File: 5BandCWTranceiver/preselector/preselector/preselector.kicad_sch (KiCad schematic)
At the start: 80 parts, among them J1 Conn_01x06_Male, J2 Conn_01x02_Male, J3 Conn_Coaxial, J4 Conn_Coaxial, J5 Conn_01x02_Male, J6 Conn_01x02_Male, J7 Conn_01x02_Male, J8 Conn_01x02_Male, J9 Conn_Coaxial, K1 G5V-2, K2 G5V-2, K3 G5V-2, K4 G5V-2, K5 G5V-2, Q1 MMBT3904, Q2 MMBT3904, Q3 MMBT3904, Q4 MMBT3904, Q5 MMBT3904

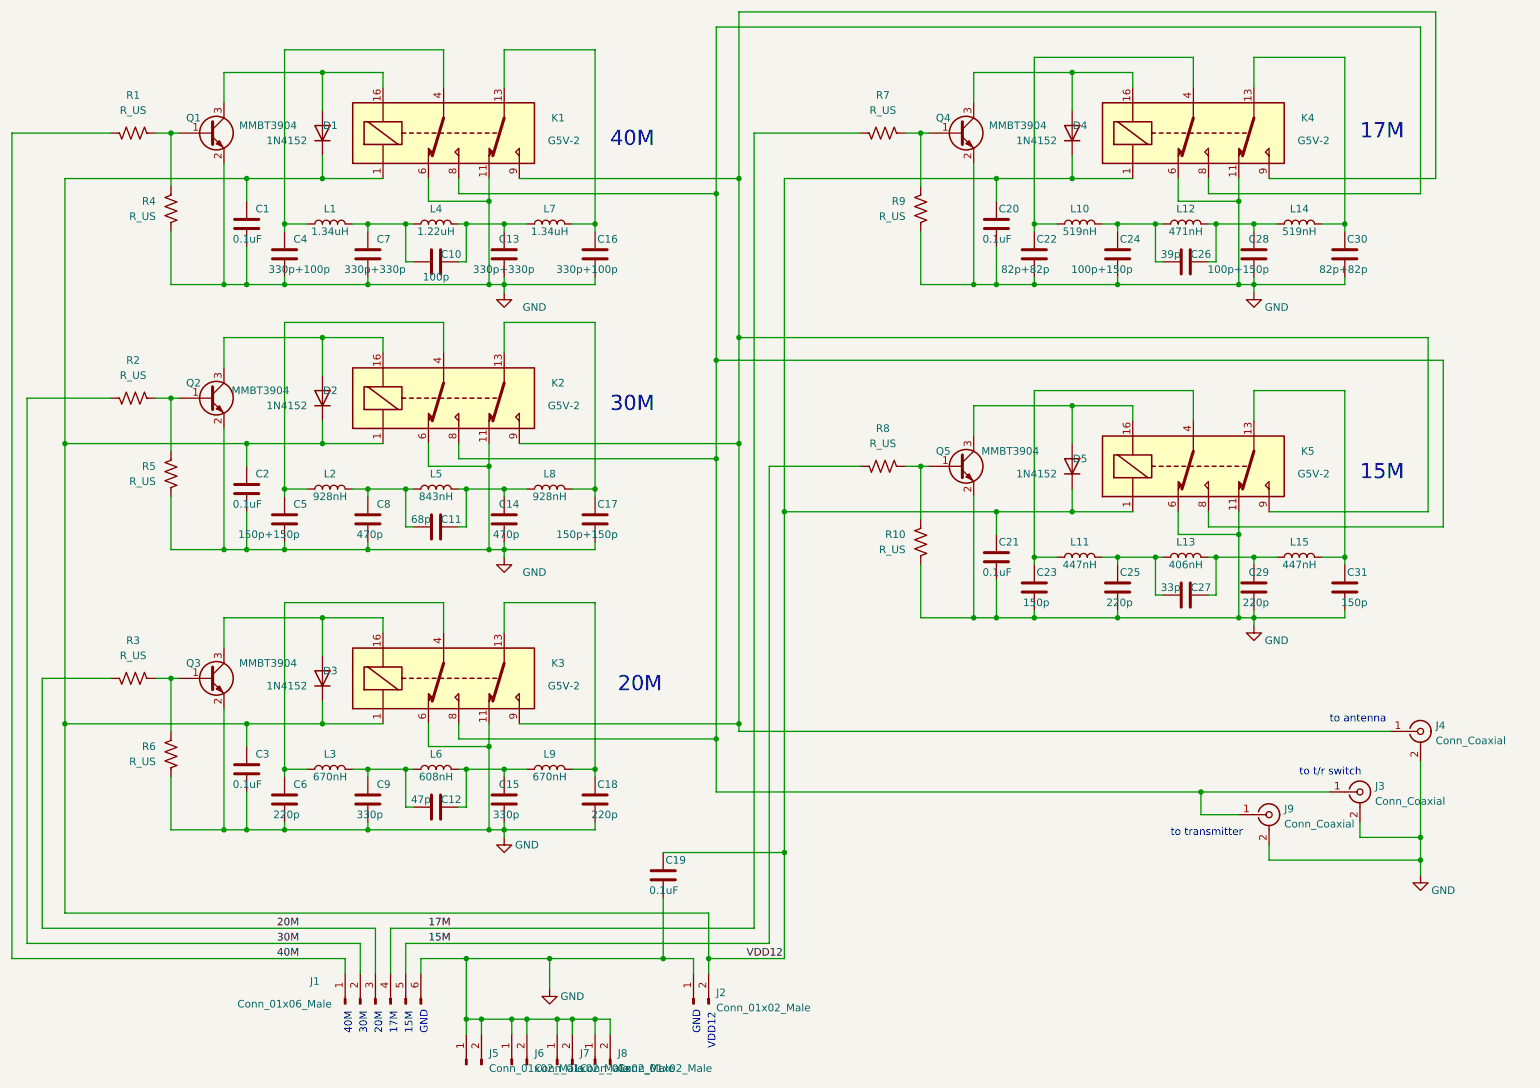
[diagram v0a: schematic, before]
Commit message: Corrected LPF; add Preselector
Fixed circuit design error on LPF regarding relay connections; first pass at adding preselctor schematic
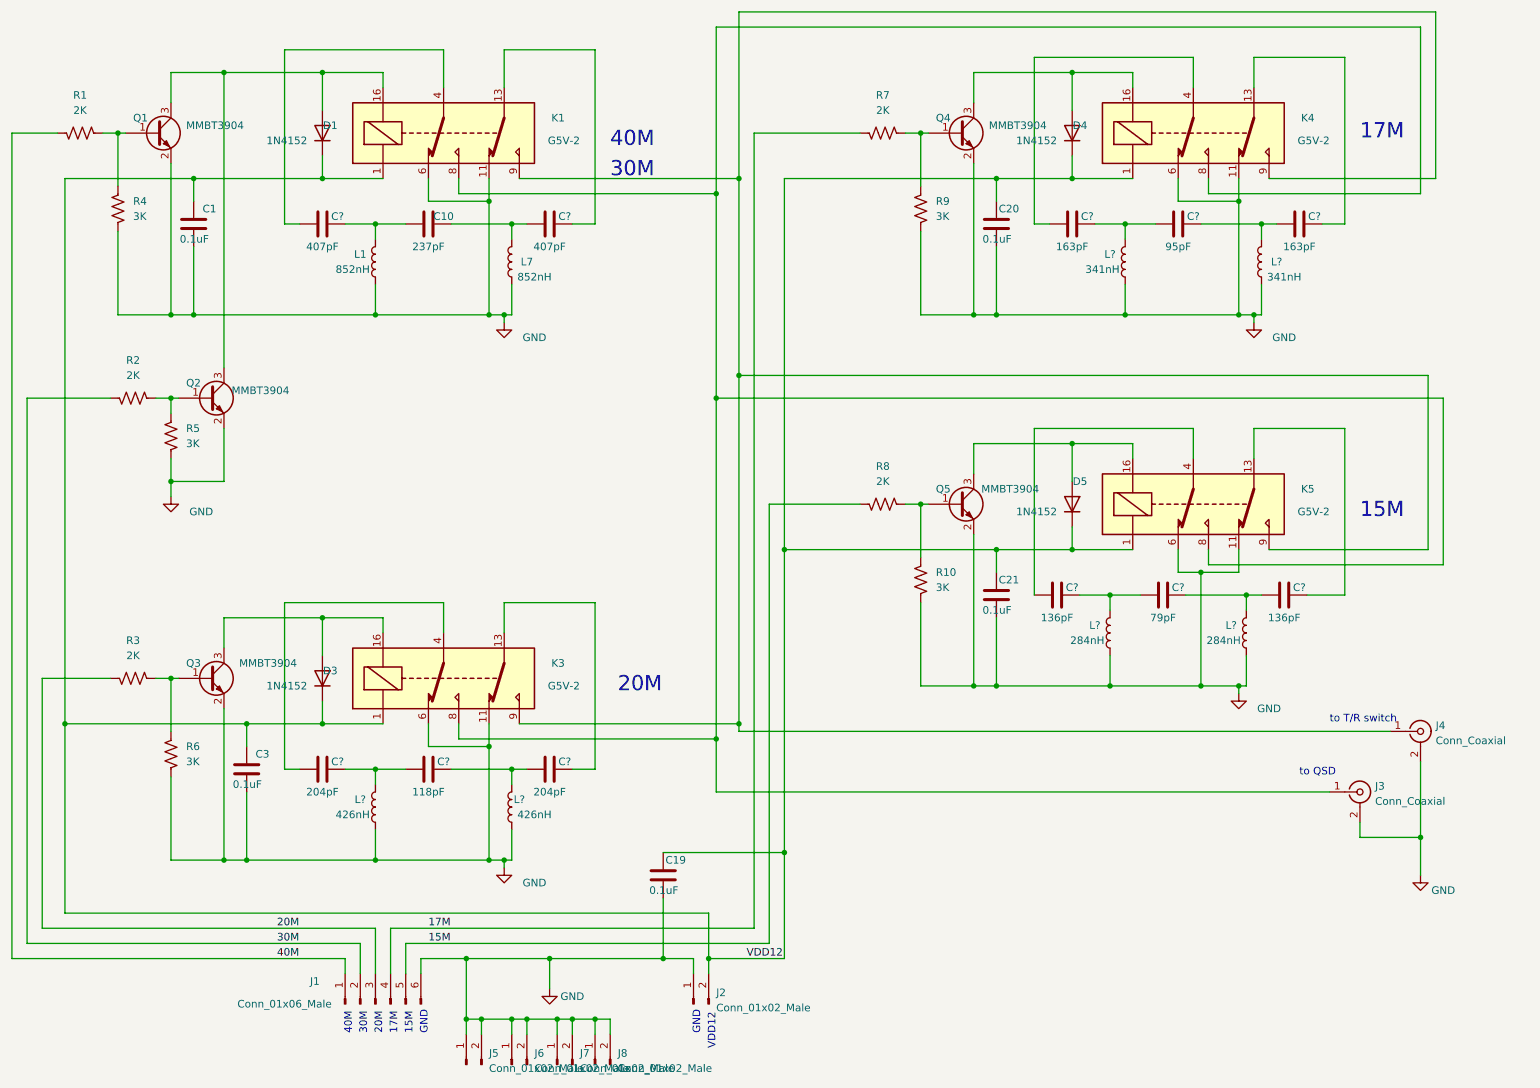
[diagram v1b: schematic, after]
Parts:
- removed C11: 68p, Capacitor_SMD:C_0805_2012Metric_Pad1.18x1.45mm_HandSolder, symbol Device:C
- removed C12: 47p, Capacitor_SMD:C_0805_2012Metric_Pad1.18x1.45mm_HandSolder, symbol Device:C
- removed C13, C7: 330p+330p, Capacitor_SMD:C_0805_2012Metric_Pad1.18x1.45mm_HandSolder, symbol Device:C
- removed C14, C8: 470p, Capacitor_SMD:C_0805_2012Metric_Pad1.18x1.45mm_HandSolder, symbol Device:C
- removed C15, C9: 330p, Capacitor_SMD:C_0805_2012Metric_Pad1.18x1.45mm_HandSolder, symbol Device:C
- removed C16, C4: 330p+100p, Capacitor_SMD:C_0805_2012Metric_Pad1.18x1.45mm_HandSolder, symbol Device:C
- removed C17, C5: 150p+150p, Capacitor_SMD:C_0805_2012Metric_Pad1.18x1.45mm_HandSolder, symbol Device:C
- removed C18, C25, C29, C6: 220p, Capacitor_SMD:C_0805_2012Metric_Pad1.18x1.45mm_HandSolder, symbol Device:C
- removed C2: 0.1uF, Capacitor_SMD:C_0603_1608Metric_Pad1.08x0.95mm_HandSolder, symbol Device:C
- removed C22, C30: 82p+82p, Capacitor_SMD:C_0805_2012Metric_Pad1.18x1.45mm_HandSolder, symbol Device:C
- removed C23, C31: 150p, Capacitor_SMD:C_0805_2012Metric_Pad1.18x1.45mm_HandSolder, symbol Device:C
- removed C24, C28: 100p+150p, Capacitor_SMD:C_0805_2012Metric_Pad1.18x1.45mm_HandSolder, symbol Device:C
- removed C26: 39p, Capacitor_SMD:C_0805_2012Metric_Pad1.18x1.45mm_HandSolder, symbol Device:C
- removed C27: 33p, Capacitor_SMD:C_0805_2012Metric_Pad1.18x1.45mm_HandSolder, symbol Device:C
- removed D2: 1N4152, Diode_THT:D_DO-41_SOD81_P7.62mm_Horizontal, symbol Device:D
- removed J9: Conn_Coaxial, Connector_Coaxial:SMA_Samtec_SMA-J-P-X-ST-EM1_EdgeMount, symbol Connector:Conn_Coaxial
- removed K2: G5V-2, Relay_THT:Relay_DPDT_Omron_G5V-2, symbol Relay:G5V-2
- removed L10, L14: 519nH, Inductor_THT:L_Toroid_Vertical_L13.0mm_W6.5mm_P5.60mm, symbol Device:L
- removed L11, L15: 447nH, Inductor_THT:L_Toroid_Vertical_L13.0mm_W6.5mm_P5.60mm, symbol Device:L
- removed L12: 471nH, Inductor_THT:L_Toroid_Vertical_L13.0mm_W6.5mm_P5.60mm, symbol Device:L
- removed L13: 406nH, Inductor_THT:L_Toroid_Vertical_L13.0mm_W6.5mm_P5.60mm, symbol Device:L
- removed L2, L8: 928nH, Inductor_THT:L_Toroid_Vertical_L13.0mm_W6.5mm_P5.60mm, symbol Device:L
- removed L3, L9: 670nH, Inductor_THT:L_Toroid_Vertical_L13.0mm_W6.5mm_P5.60mm, symbol Device:L
- removed L4: 1.22uH, Inductor_THT:L_Toroid_Vertical_L13.0mm_W6.5mm_P5.60mm, symbol Device:L
- removed L5: 843nH, Inductor_THT:L_Toroid_Vertical_L13.0mm_W6.5mm_P5.60mm, symbol Device:L
- removed L6: 608nH, Inductor_THT:L_Toroid_Vertical_L13.0mm_W6.5mm_P5.60mm, symbol Device:L
- added C? (x2): 204pF, Capacitor_SMD:C_0805_2012Metric_Pad1.18x1.45mm_HandSolder, symbol Device:C
- added C?: 95pF, Capacitor_SMD:C_0805_2012Metric_Pad1.18x1.45mm_HandSolder, symbol Device:C
- added C?: 118pF, Capacitor_SMD:C_0805_2012Metric_Pad1.18x1.45mm_HandSolder, symbol Device:C
- added C? (x2): 136pF, Capacitor_SMD:C_0805_2012Metric_Pad1.18x1.45mm_HandSolder, symbol Device:C
- added C? (x2): 163pF, Capacitor_SMD:C_0805_2012Metric_Pad1.18x1.45mm_HandSolder, symbol Device:C
- added C?: 79pF, Capacitor_SMD:C_0805_2012Metric_Pad1.18x1.45mm_HandSolder, symbol Device:C
- added C? (x2): 407pF, Capacitor_SMD:C_0805_2012Metric_Pad1.18x1.45mm_HandSolder, symbol Device:C
- added L? (x2): 341nH, Inductor_THT:L_Toroid_Vertical_L13.0mm_W6.5mm_P5.60mm, symbol Device:L
- added L? (x2): 426nH, Inductor_THT:L_Toroid_Vertical_L13.0mm_W6.5mm_P5.60mm, symbol Device:L
- added L? (x2): 284nH, Inductor_THT:L_Toroid_Vertical_L13.0mm_W6.5mm_P5.60mm, symbol Device:L
- C10: value 100p -> 237pF
- L1, L7: value 1.34uH -> 852nH
- R1, R2, R3, R7, R8: value R_US -> 2K
- R10, R4, R5, R6, R9: value R_US -> 3K
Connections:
- net GND: now also L1.2, L7.2, L?.2, L?.2, L?.2, L?.2, L?.2, L?.2
- net at K4.13: now also C?.1
- net at K3.13: now also C?.1
- net at K3.4: now also C?.2
- net at C10.1: now also L7.1, C?.2; no longer L7.2
- net at C10.2, L1.1: now also C?.1
- net at D1.2 (A), K1.16, Q1.3 (C): now also Q2.3 (C)
- net at K5.13: now also C?.1
- net at K5.4: now also C?.2
- net at K4.4: now also C?.2
- net at K1.4: now also C?.2; no longer L1.2
- net at K1.13: now also C?.1; no longer L7.1
- new net: C?.1, C?.2, L?.1 (x6)
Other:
- note added: "to QSD"
- note added: "to T/R switch"
- note removed: "to antenna"
- note removed: "to t/r switch"
- note removed: "to transmitter"
- moved on the sheet: C1, C10, C21, D5, K5, L1, L7, Q1, Q5, R1, R10, R4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

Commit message: Added T/R Switch
Added T/R switch and updated preselector.
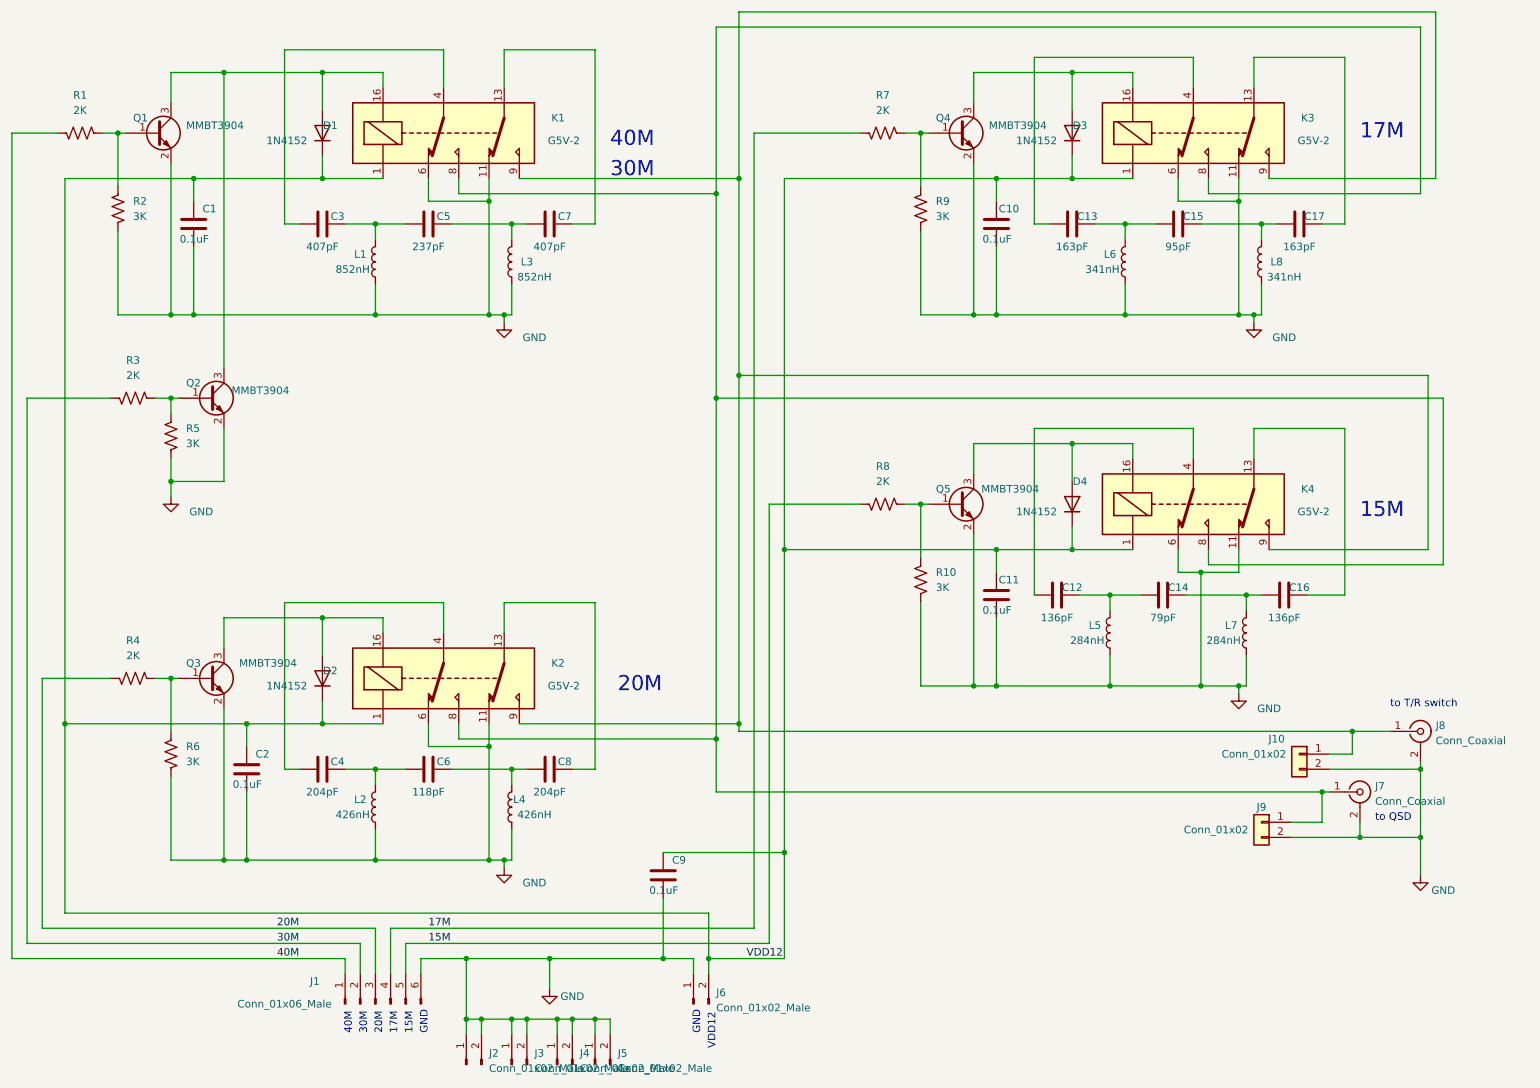
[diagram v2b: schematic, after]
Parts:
- added J10, J9: Conn_01x02, Connector_PinHeader_2.54mm:PinHeader_1x02_P2.54mm_Vertical, symbol Connector_Generic:Conn_01x02
- gave numbers to parts that had none: 17
- renumbered C20 to C10, C21 to C11, C3 to C2, C10 to C5, C19 to C9, D3 to D2, D4 to D3, D5 to D4, J5 to J2, J6 to J3, J7 to J4, J8 to J5, J2 to J6, J3 to J7, J4 to J8, K3 to K2, K4 to K3, K5 to K4, L7 to L3, R4 to R2, R2 to R3, R3 to R4
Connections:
- net GND: now also J10.2 (Pin_2), J9.2 (Pin_2)
- net at J7.1 (In), K1.8, K2.8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: now also J9.1 (Pin_1)
- net at J8.1 (In), K1.9, K2.9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: now also J10.1 (Pin_1)
